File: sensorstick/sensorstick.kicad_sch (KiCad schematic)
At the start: 20 parts, among them J1 U217-04XN-XXR84, U1 ESP32-C3_SUPERMINI, U2 SGP30, U3 SHT4x, U4 SCD40-D-R2, U5 TPS71533__SC70, U6 2N7002DW

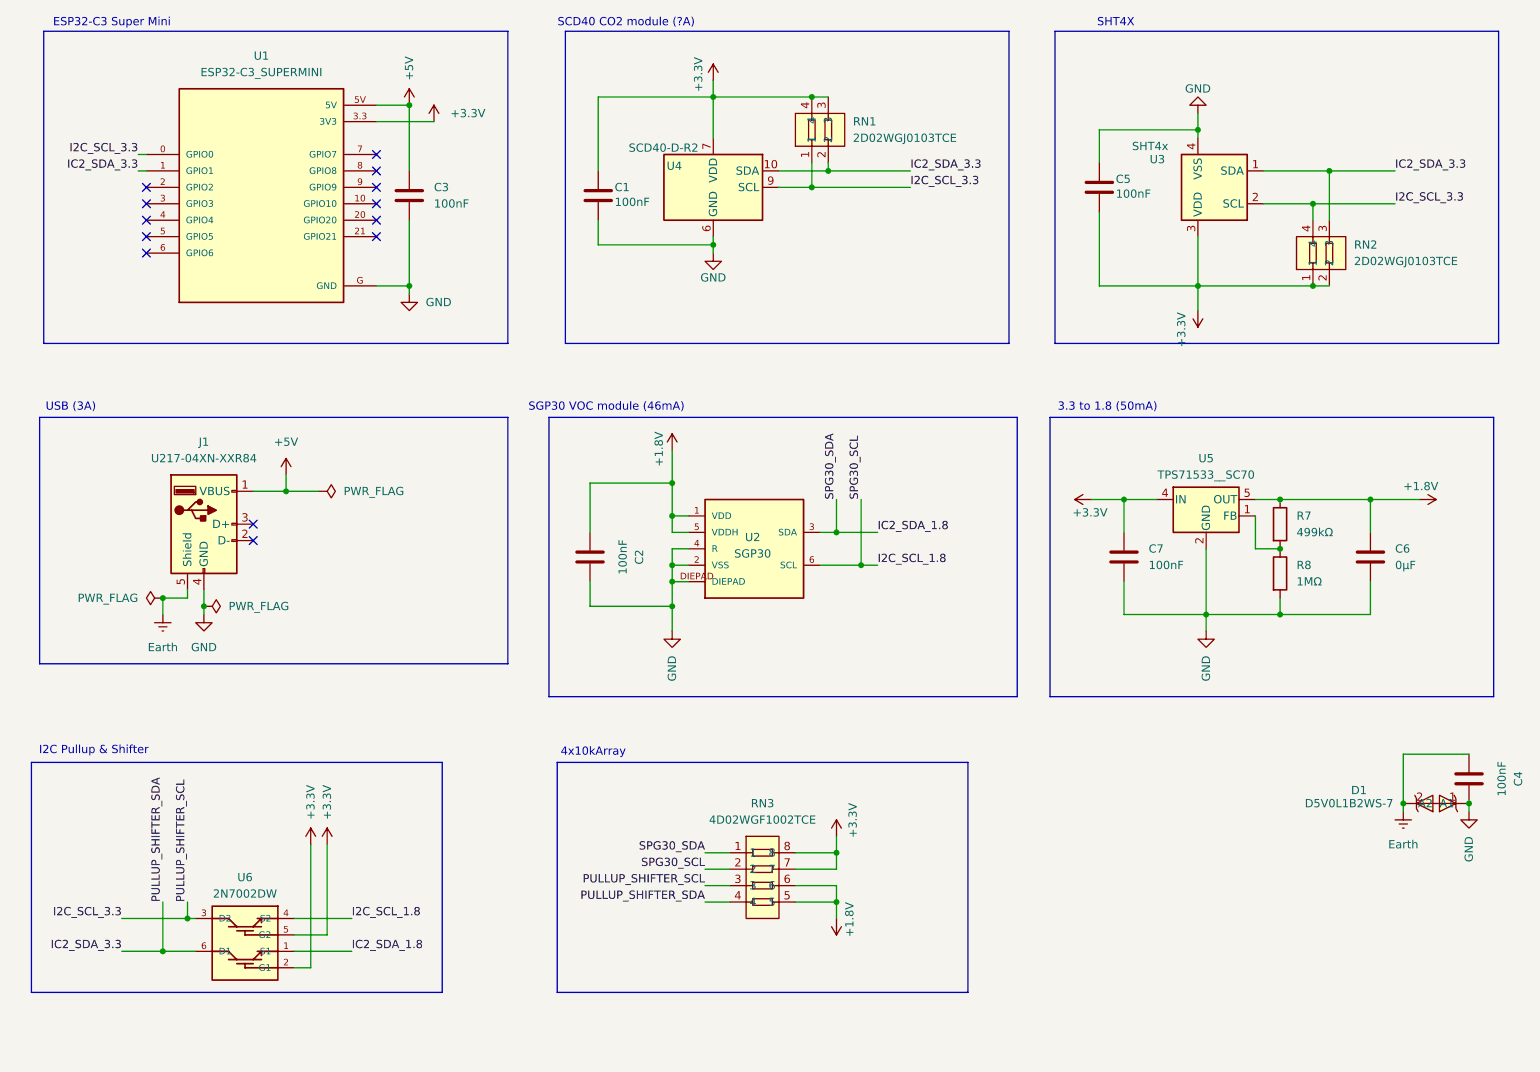
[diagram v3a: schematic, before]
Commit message: added jcsc part numbers
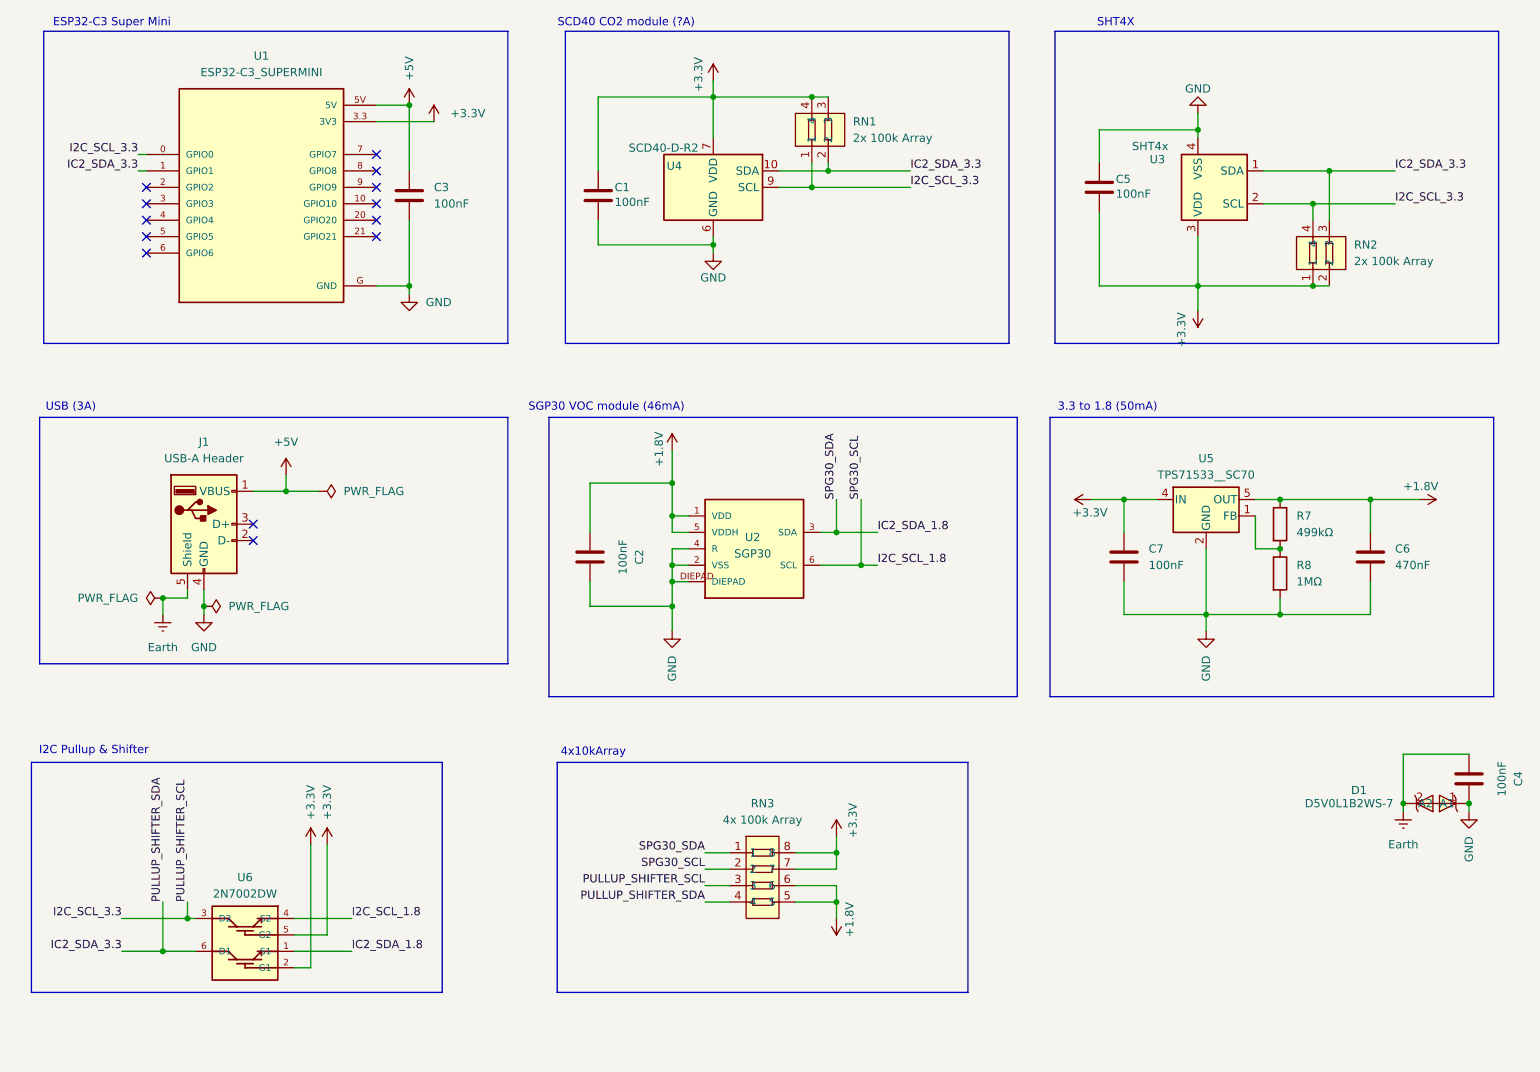
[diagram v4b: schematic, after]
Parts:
- C1, C5: LCSC C14663 -> C1591
- C6: value 0μF -> 470nF; LCSC (none) -> C1623
- C7: LCSC (none) -> C1591
- D1: LCSC (none) -> C182013
- J1: value U217-04XN-XXR84 -> USB-A Header
- R7: LCSC (none) -> C407576
- R8: LCSC (none) -> C9900163442
- RN1, RN2: value 2D02WGJ0103TCE -> 2x 100k Array; LCSC (none) -> C2765527
- RN3: value 4D02WGF1002TCE -> 4x 100k Array; LCSC (none) -> C414600
- U5: LCSC (none) -> C571193
- U6: LCSC (none) -> C232839
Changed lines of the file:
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@@
 			)
 		)
+		(property "LCSC" "C182013"
+			(at 233.172 146.558 0)
+			(effects
+				(font
+					(size 1.27 1.27)
+				)
+				(hide yes)
+			)
+		)
 		(pin "2"
 		)
@@
 			)
 		)
-		(property "LCSC" "C14663"
+		(property "LCSC" "C1591"
 			(at 119.38 53.3399 0)
 			(effects
@@
 			)
 		)
-		(property "Value" "U217-04XN-XXR84"
+		(property "Value" "USB-A Header"
 			(at 54.61 95.25 0)
 			(effects
@@
 			)
 		)
-		(property "Value" "2D02WGJ0103TCE"
+		(property "Value" "2x 100k Array"
 			(at 232.41 64.7699 90)
 			(effects
@@
 			)
 		)
+		(property "LCSC" "C2765527"
+			(at 232.41 62.2299 0)
+			(effects
+				(font
+					(size 1.27 1.27)
+				)
+				(hide yes)
+			)
+		)
 		(pin "4"
 		)
@@
 			)
 		)
-		(property "Value" "0μF"
+		(property "Value" "470nF"
 			(at 238.76 111.7599 0)
 			(effects
@@
 			)
 		)
-		(property "Datasheet" "~"
+		(property "Datasheet" "https://www.lcsc.com/datasheet/C1623.pdf"
 			(at 234.95 110.49 0)
 			(effects
@@
 			)
 		)
+		(property "LCSC" "C1623"
+			(at 238.76 109.2199 0)
+			(effects
+				(font
+					(size 1.27 1.27)
+				)
+				(hide yes)
+			)
+		)
 		(pin "2"
 		)
@@
 			)
 		)
-		(property "LCSC" "C14663"
+		(property "LCSC" "C1591"
 			(at 196.85 52.0699 0)
 			(effects
@@
 			)
 		)
+		(property "LCSC" "C1591"
+			(at 200.66 109.2199 0)
+			(effects
+				(font
+					(size 1.27 1.27)
+				)
+				(hide yes)
+			)
+		)
 		(pin "2"
 		)
@@
 			)
 		)
+		(property "LCSC" "C571193"
+			(at 209.55 95.25 0)
+			(effects
+				(font
+					(size 1.27 1.27)
+				)
+				(hide yes)
+			)
+		)
 		(pin "5"
 		)
@@
 			)
 		)
-		(property "Datasheet" ""
+		(property "Datasheet" "https://www.lcsc.com/datasheet/C232839.pdf"
 			(at 60.96 168.91 0)
 			(effects
@@
 			)
 		)
+		(property "LCSC" "C232839"
+			(at 60.96 160.02 0)
+			(effects
+				(font
+					(size 1.27 1.27)
+				)
+				(hide yes)
+			)
+		)
 		(pin "5"
 		)
@@
 			)
 		)
-		(property "Value" "2D02WGJ0103TCE"
+		(property "Value" "2x 100k Array"
 			(at 154.94 45.7199 90)
 			(effects
@@
 			)
 		)
+		(property "LCSC" "C2765527"
+			(at 154.94 43.1799 0)
+			(effects
+				(font
+					(size 1.27 1.27)
+				)
+				(hide yes)
+			)
+		)
 		(pin "4"
 		)
@@
 			)
 		)
+		(property "LCSC" "C9900163442"
+			(at 223.52 111.7599 0)
+			(effects
+				(font
+					(size 1.27 1.27)
+				)
+				(hide yes)
+			)
+		)
 		(pin "1"
 		)
@@
 			)
 		)
+		(property "LCSC" "C407576"
+			(at 223.52 104.1399 0)
+			(effects
+				(font
+					(size 1.27 1.27)
+				)
+				(hide yes)
+			)
+		)
 		(pin "1"
 		)
@@
 			)
 		)
-		(property "Value" "4D02WGF1002TCE"
+		(property "Value" "4x 100k Array"
 			(at 140.97 151.13 0)
 			(effects
@@
 			(effects
 				(font
+					(size 1.27 1.27)
+				)
+				(hide yes)
+			)
+		)
+		(property "LCSC" "C414600"
+			(at 140.97 148.59 0)
+			(effects
+				(font

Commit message: changed 3,3 to 1,8 module and i2c level shifter
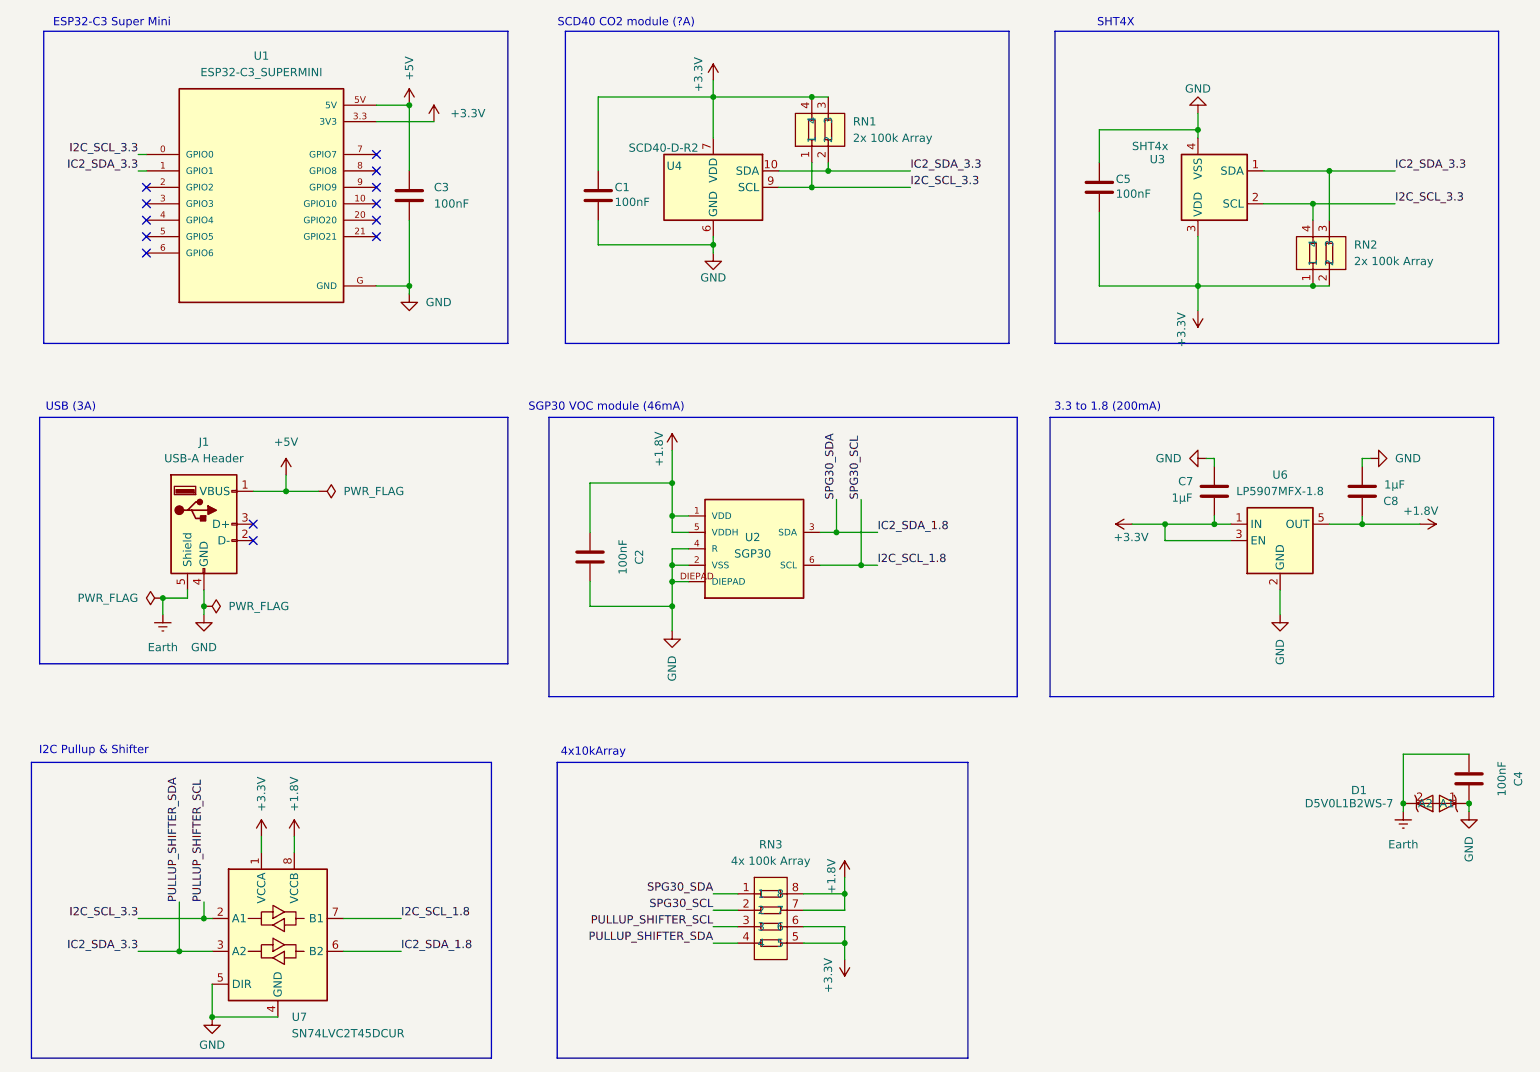
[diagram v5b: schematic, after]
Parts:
- removed C6: 470nF, Capacitor_SMD:C_0603_1608Metric, symbol Device:C
- removed R7: 499kΩ, Resistor_SMD:R_0603_1608Metric, symbol Device:R
- removed R8: 1MΩ, Resistor_SMD:R_0603_1608Metric, symbol Device:R
- removed U5: TPS71533__SC70, Package_TO_SOT_SMD:SOT-353_SC-70-5, symbol Regulator_Linear:TPS71533__SC70
- removed U6: 2N7002DW, 2N7002DW:SOT363, symbol 2N7002DW:2N7002DW
- added C8: 1µF, Capacitor_SMD:C_0603_1608Metric, symbol Device:C
- added U6: LP5907MFX-1.8, Package_TO_SOT_SMD:SOT-23-5, symbol Regulator_Linear:LP5907MFX-1.8
- added U7: SN74LVC2T45DCUR, Package_SO:VSSOP-8_2.3x2mm_P0.5mm, symbol Logic_LevelTranslator:SN74LVC2T45DCUR
- C7: value 100nF -> 1µF; LCSC C1591 -> C458914
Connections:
- net +1.8V: now also RN3.7, RN3.8, C8.2, U6.5 (OUT), U7.8 (VCCB); no longer RN3.5, RN3.6
- net +3.3V: now also RN3.5, RN3.6, U6.1 (IN), U6.3 (EN), U7.1 (VCCA); no longer RN3.7, RN3.8
- net GND: now also C8.1, U6.2 (GND), U7.4 (GND), U7.5 (DIR)
- net I2C_SCL_1.8: now also U7.7 (B1)
- net I2C_SCL_3.3: now also U7.2 (A1)
- net IC2_SDA_1.8: now also U7.6 (B2)
- net IC2_SDA_3.3: now also U7.3 (A2)
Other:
- note added: "3.3 to 1.8 (200mA)"
- note removed: "3.3 to 1.8 (50mA)"
- moved on the sheet: C7, RN3

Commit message: changed rev number to 2
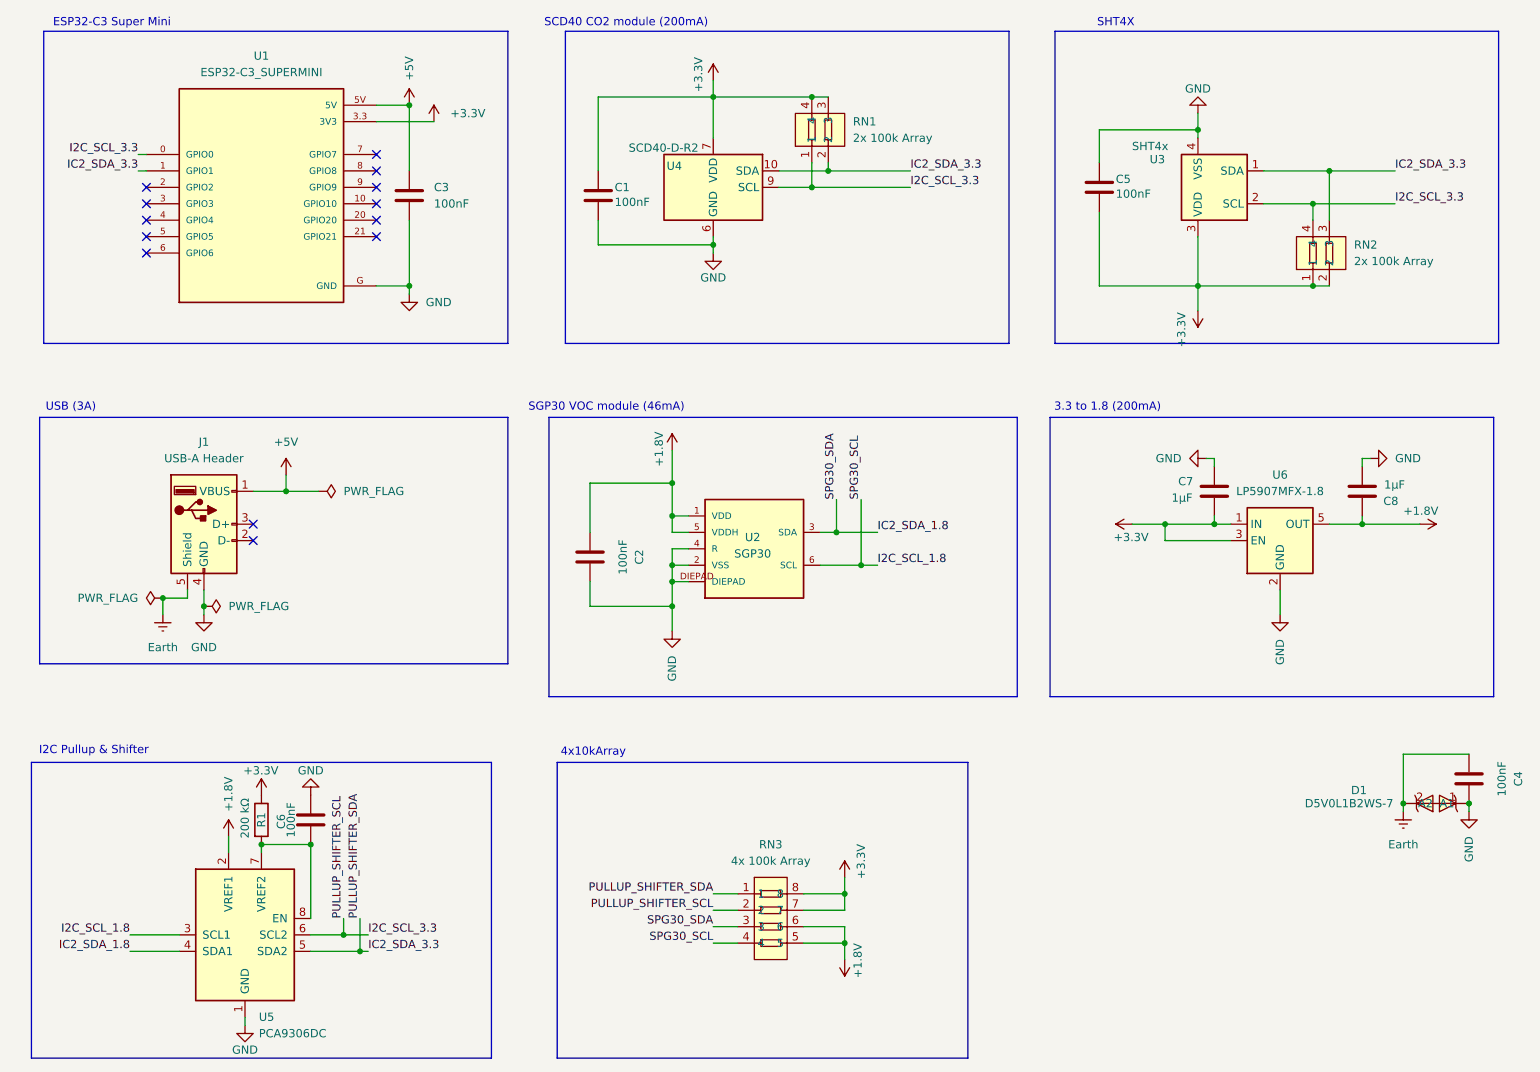
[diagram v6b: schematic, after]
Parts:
- removed U7: SN74LVC2T45DCUR, Package_SO:VSSOP-8_2.3x2mm_P0.5mm, symbol Logic_LevelTranslator:SN74LVC2T45DCUR
- added C6: 100nF, Capacitor_SMD:C_0603_1608Metric, symbol Device:C
- added R1: 200 kΩ, Resistor_SMD:R_0603_1608Metric, symbol Device:R
- added U5: PCA9306DC, Package_SO:VSSOP-8_2.3x2mm_P0.5mm, symbol Interface:PCA9306DC
- U6: LCSC C92498 -> (none)
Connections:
- net +1.8V: now also RN3.5, RN3.6, U5.2 (VREF1); no longer RN3.7, RN3.8
- net +3.3V: now also RN3.7, RN3.8, R1.1; no longer RN3.5, RN3.6
- net GND: now also C6.2, U5.1 (GND)
- net I2C_SCL_1.8: now also RN3.4, U5.3 (SCL1); no longer RN3.2
- net I2C_SCL_3.3: now also RN3.2, U5.6 (SCL2); no longer RN3.3
- net IC2_SDA_1.8: now also RN3.3, U5.4 (SDA1); no longer RN3.1
- net IC2_SDA_3.3: now also RN3.1, U5.5 (SDA2); no longer RN3.4
- new net: C6.1, R1.2, U5.7 (VREF2), U5.8 (EN)
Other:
- note added: "SCD40 CO2 module (200mA)"
- note removed: "SCD40 CO2 module (?A)"
